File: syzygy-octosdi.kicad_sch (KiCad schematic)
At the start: 22 parts, among them CN1 QTH-020-01-F-D-DP-A, X1 SX7DF148_500B20F30DNN

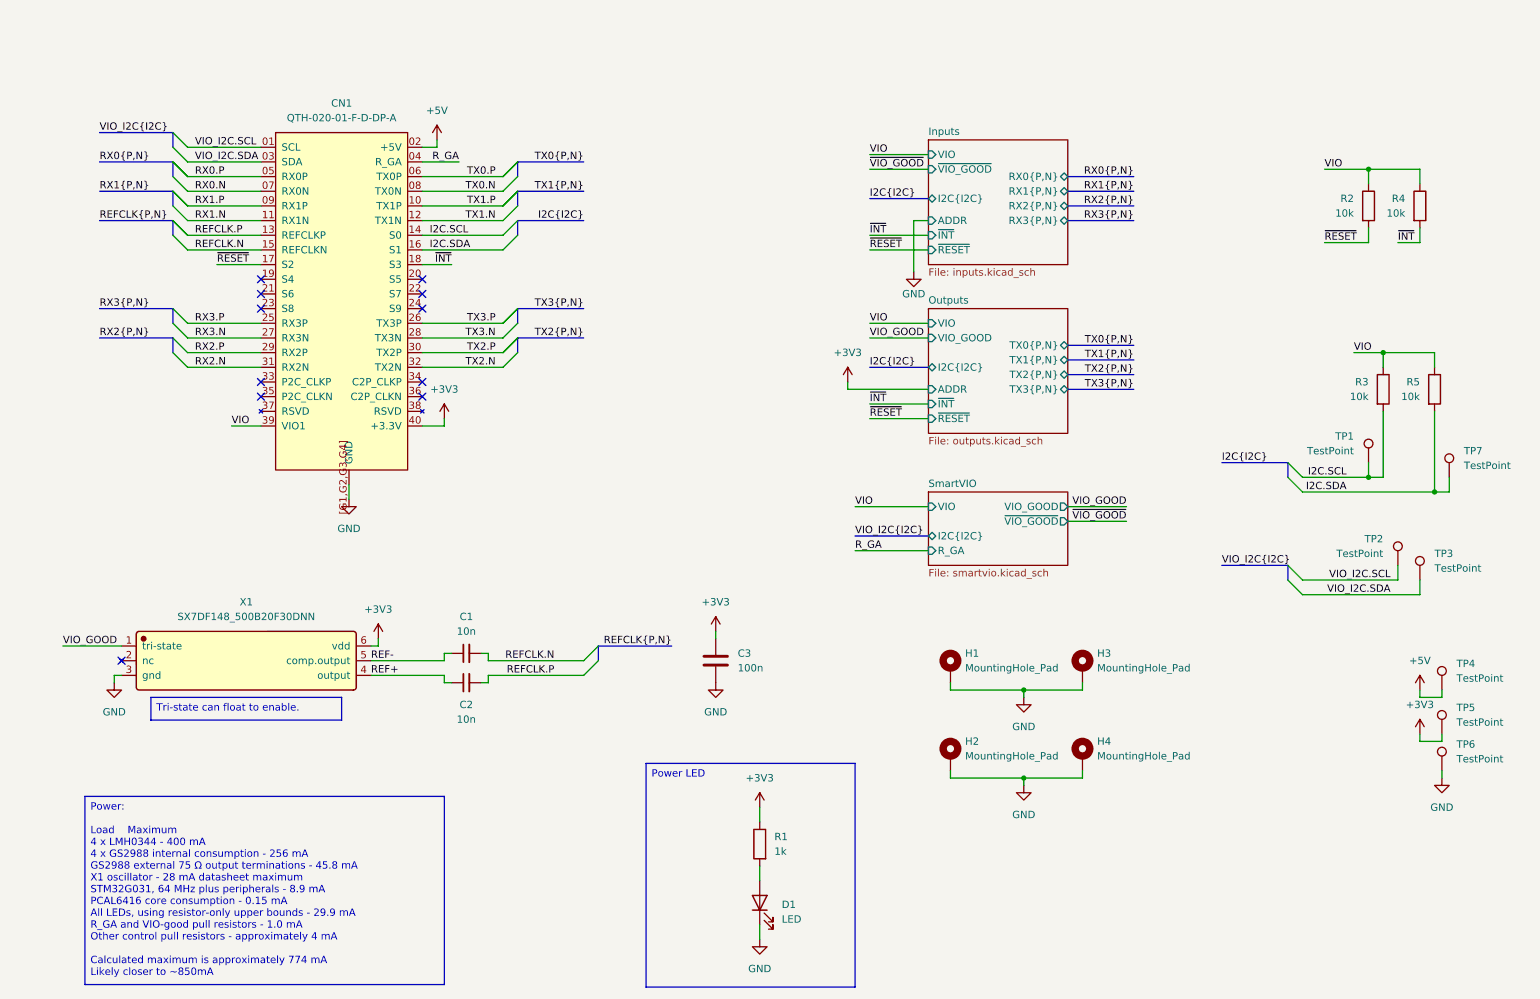
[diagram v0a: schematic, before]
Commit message: add some larger bypass caps to the cable drivers
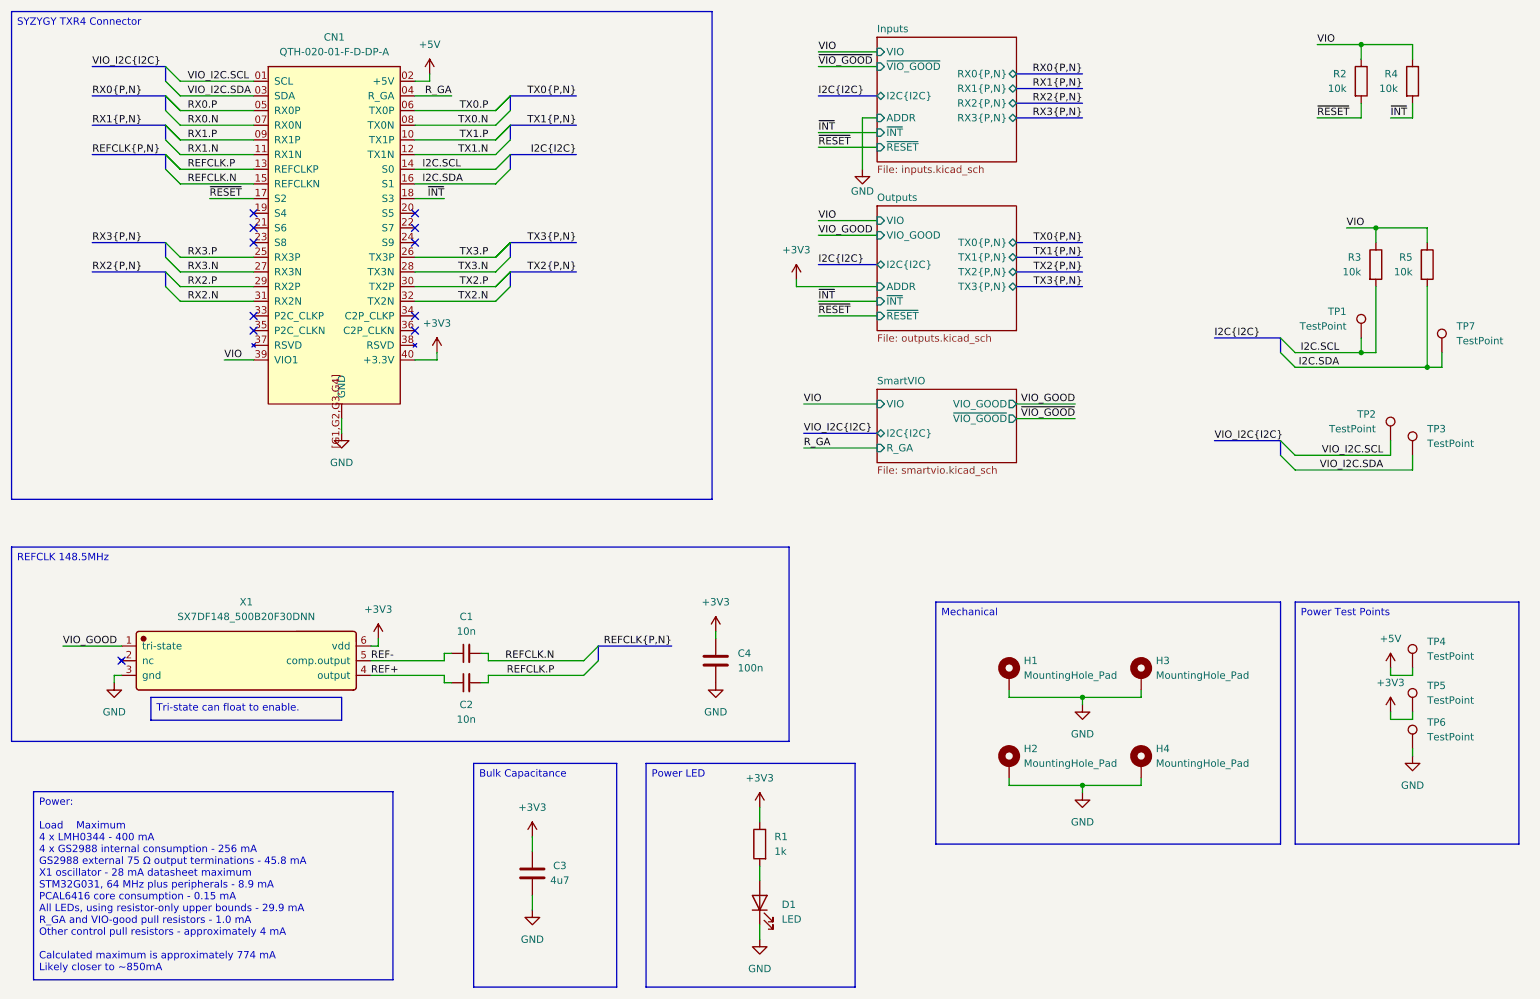
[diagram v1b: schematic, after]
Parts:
- added C3: 4u7, Capacitor_SMD:C_0603_1608Metric, symbol Device:C
- renumbered C3 to C4
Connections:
- net +3V3: now also C3.1
- net GND: now also C3.2
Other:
- moved on the sheet: CN1, H1, H2, H3, H4, R2, R3, R4, R5, TP1, TP2, TP3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

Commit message: specify skus for parts
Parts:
- C1, C2: LCSC (none) -> C15195
- C3: LCSC (none) -> C69335
- C4: LCSC (none) -> C282519
- R1: LCSC (none) -> C21190
- R2, R3, R4, R5: LCSC (none) -> C25804
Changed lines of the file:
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@@
 			)
 		)
+		(property "LCSC" "C15195"
+			(at 95.25 135.89 90)
+			(hide yes)
+			(show_name no)
+			(do_not_autoplace no)
+			(effects
+				(font
+					(size 1.27 1.27)
+				)
+			)
+		)
 		(pin "2"
 		)
@@
 			)
 		)
+		(property "LCSC" "C25804"
+			(at 252.73 63.5 0)
+			(hide yes)
+			(show_name no)
+			(do_not_autoplace no)
+			(effects
+				(font
+					(size 1.27 1.27)
+				)
+			)
+		)
 		(pin "1"
 		)
@@
 			)
 		)
+		(property "LCSC" "C25804"
+			(at 261.62 63.5 0)
+			(hide yes)
+			(show_name no)
+			(do_not_autoplace no)
+			(effects
+				(font
+					(size 1.27 1.27)
+				)
+			)
+		)
 		(pin "1"
 		)
@@
 			)
 		)
+		(property "LCSC" "C15195"
+			(at 95.25 130.81 90)
+			(hide yes)
+			(show_name no)
+			(do_not_autoplace no)
+			(effects
+				(font
+					(size 1.27 1.27)
+				)
+			)
+		)
 		(pin "2"
 		)
@@
 			)
 		)
+		(property "LCSC" "C25804"
+			(at 259.08 31.75 0)
+			(hide yes)
+			(show_name no)
+			(do_not_autoplace no)
+			(effects
+				(font
+					(size 1.27 1.27)
+				)
+			)
+		)
 		(pin "1"
 		)
@@
 			)
 		)
+		(property "LCSC" "C69335"
+			(at 106.68 168.91 0)
+			(hide yes)
+			(show_name no)
+			(do_not_autoplace no)
+			(effects
+				(font
+					(size 1.27 1.27)
+				)
+			)
+		)
 		(pin "2"
 		)
@@
 			)
 		)
+		(property "LCSC" "C25804"
+			(at 250.19 31.75 0)
+			(hide yes)
+			(show_name no)
+			(do_not_autoplace no)
+			(effects
+				(font
+					(size 1.27 1.27)
+				)
+			)
+		)
 		(pin "1"
 		)
@@
 			)
 		)
+		(property "LCSC" "C282519"
+			(at 138.43 132.08 0)
+			(hide yes)
+			(show_name no)
+			(do_not_autoplace no)
+			(effects
+				(font
+					(size 1.27 1.27)
+				)
+			)
+		)
 		(pin "1"
 		)
@@
 			(at 146.05 163.83 0)
 			(hide yes)
+			(show_name no)
+			(do_not_autoplace no)
+			(effects
+				(font
+					(size 1.27 1.27)
+				)
+			)
+		)
+		(property "LCSC" "C21190"
+			(at 146.05 163.83 0)
+			(hide yes)

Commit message: specify led colours
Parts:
- D1: value LED -> LED Red
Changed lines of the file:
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@@
 			)
 		)
-		(property "Value" "LED"
+		(property "Value" "LED Red"
 			(at 149.86 176.8474 90)
 			(show_name no)

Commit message: add vio test point
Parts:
- added TP6: TestPoint, TestPoint:TestPoint_Pad_D1.0mm, symbol Connector:TestPoint
- renumbered TP6 to TP7, TP7 to TP8
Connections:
- net VIO: now also TP6.1
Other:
- moved on the sheet: TP7
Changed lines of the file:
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@@
 	(wire
 		(pts
+			(xy 254 148.59) (xy 259.08 148.59)
+		)
+		(stroke
+			(width 0)
+			(type default)
+		)
+	)
+	(wire
+		(pts
 			(xy 259.08 25.4) (xy 250.19 25.4)
 		)
@@
 	(wire
 		(pts
-			(xy 259.08 147.32) (xy 259.08 148.59)
+			(xy 259.08 154.94) (xy 259.08 156.21)
 		)
 		(stroke
@@
 	(wire
 		(pts
+			(xy 259.08 148.59) (xy 259.08 147.32)
+		)
+		(stroke
+			(width 0)
+			(type default)
+		)
+	)
+	(wire
+		(pts
 			(xy 146.05 167.64) (xy 146.05 170.18)
 		)
@@
 		)
 	)
+	(label "VIO"
+		(at 254 148.59 0)
+		(effects
+			(font
+				(size 1.27 1.27)
+			)
+			(justify left bottom)
+		)
+	)
 	(label "RX1{P,N}"
 		(at 201.93 33.02 180)
@@
 	)
 	(symbol
+		(lib_id "Connector:TestPoint")
+		(at 259.08 147.32 0)
+		(unit 1)
+		(body_style 1)
+		(exclude_from_sim no)
+		(in_bom no)
+		(on_board yes)
+		(in_pos_files yes)
+		(dnp no)
+		(fields_autoplaced yes)
+		(property "Reference" "TP6"
+			(at 261.62 142.7479 0)
+			(show_name no)
+			(do_not_autoplace no)
+			(effects
+				(font
+					(size 1.27 1.27)
+				)
+				(justify left)
+			)
+		)
+		(property "Value" "TestPoint"
+			(at 261.62 145.2879 0)
+			(show_name no)
+			(do_not_autoplace no)
+			(effects
+				(font
+					(size 1.27 1.27)
+				)
+				(justify left)
+			)
+		)
+		(property "Footprint" "TestPoint:TestPoint_Pad_D1.0mm"
+			(at 264.16 147.32 0)
+			(hide yes)
+			(show_name no)
+			(do_not_autoplace no)
+			(effects
+				(font
+					(size 1.27 1.27)
+				)
+			)
+		)
+		(property "Datasheet" ""
+			(at 264.16 147.32 0)
+			(hide yes)
+			(show_name no)
+			(do_not_autoplace no)
+			(effects
+				(font
+					(size 1.27 1.27)
+				)
+			)
+		)
+		(property "Description" "test point"
+			(at 259.08 147.32 0)
+			(hide yes)
+			(show_name no)
+			(do_not_autoplace no)
+			(effects
+				(font
+					(size 1.27 1.27)
+				)
+			)
+		)
+		(pin "1"
+		)
+		(instances
+			(project "syzygy-octosdi"
+				(path "/cb0cdcc9-6b9b-4b74-8146-9043de7999b1"
+					(reference "TP6")
+					(unit 1)
+				)
+			)
+		)
+	)
+	(symbol
 		(lib_id "Device:C_Small")
 		(at 95.25 130.81 90)
@@
 	(symbol
 		(lib_id "Connector:TestPoint")
-		(at 259.08 147.32 0)
+		(at 259.08 154.94 0)
 		(unit 1)
 		(body_style 1)
@@
 		(dnp no)
 		(fields_autoplaced yes)
-		(property "Reference" "TP6"
-			(at 261.62 142.7479 0)
+		(property "Reference" "TP7"
+			(at 261.62 150.3679 0)
 			(show_name no)
 			(do_not_autoplace no)
@@
 		)
 		(property "Value" "TestPoint"
-			(at 261.62 145.2879 0)
+			(at 261.62 152.9079 0)
 			(show_name no)
 			(do_not_autoplace no)
@@
 		)
 		(property "Footprint" "TestPoint:TestPoint_Pad_D1.0mm"
-			(at 264.16 147.32 0)
+			(at 264.16 154.94 0)
 			(hide yes)
 			(show_name no)
@@
 		)
 		(property "Datasheet" ""
-			(at 264.16 147.32 0)
+			(at 264.16 154.94 0)
 			(hide yes)
 			(show_name no)
@@
 		)
 		(property "Description" "test point"
-			(at 259.08 147.32 0)
+			(at 259.08 154.94 0)
 			(hide yes)
 			(show_name no)
@@
 			(project "syzygy-octosdi"
 				(path "/cb0cdcc9-6b9b-4b74-8146-9043de7999b1"
-					(reference "TP6")
+					(reference "TP7")
 					(unit 1)
 				)
@@
 	(symbol
 		(lib_id "power:GND")
-		(at 259.08 148.59 0)
+		(at 259.08 156.21 0)
 		(unit 1)
 		(body_style 1)
@@
 		(fields_autoplaced yes)
 		(property "Reference" "#PWR018"
-			(at 259.08 154.94 0)
+			(at 259.08 162.56 0)
 			(hide yes)
 			(show_name no)
@@
 		)
 		(property "Value" "GND"
-			(at 259.08 153.67 0)
+			(at 259.08 161.29 0)
 			(show_name no)
 			(do_not_autoplace no)
@@
 		)
 		(property "Footprint" ""
-			(at 259.08 148.59 0)
+			(at 259.08 156.21 0)
 			(hide yes)
 			(show_name no)
@@
 		)
 		(property "Datasheet" ""
-			(at 259.08 148.59 0)
+			(at 259.08 156.21 0)
 			(hide yes)
 			(show_name no)
@@
 		)
 		(property "Description" "Power symbol creates a global label with name \"GND\" , ground"
-			(at 259.08 148.59 0)
+			(at 259.08 156.21 0)
 			(hide yes)
 			(show_name no)
@@
 		(dnp no)
 		(fields_autoplaced yes)
-		(property "Reference" "TP7"
+		(property "Reference" "TP8"
 			(at 266.7 74.1679 0)
 			(show_name no)
@@
 			(project "syzygy-octosdi"
 				(path "/cb0cdcc9-6b9b-4b74-8146-9043de7999b1"
-					(reference "TP7")
+					(reference "TP8")
 					(unit 1)
 				)

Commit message: sku and led resistor updates following review
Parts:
- D1: LCSC (none) -> C965799
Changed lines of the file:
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@@
+			)
+		)
+		(property "LCSC" "C965799"
+			(at 146.05 173.99 90)
+			(hide yes)
+			(show_name no)
+			(do_not_autoplace no)
+			(effects
+				(font
+					(size 1.27 1.27)
+				)
 			)
 		)
